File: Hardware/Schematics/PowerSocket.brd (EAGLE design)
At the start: 100 x 50 mm, 74 parts, among them IC1 ACS712-LC, IC2 ACS712-LC, IC3 ACS712-LC, T1 BT138-V, T2 BT138-V, T3 BT138-V, T4 BT138-V, T5 BT138-V, T6 BT138-V

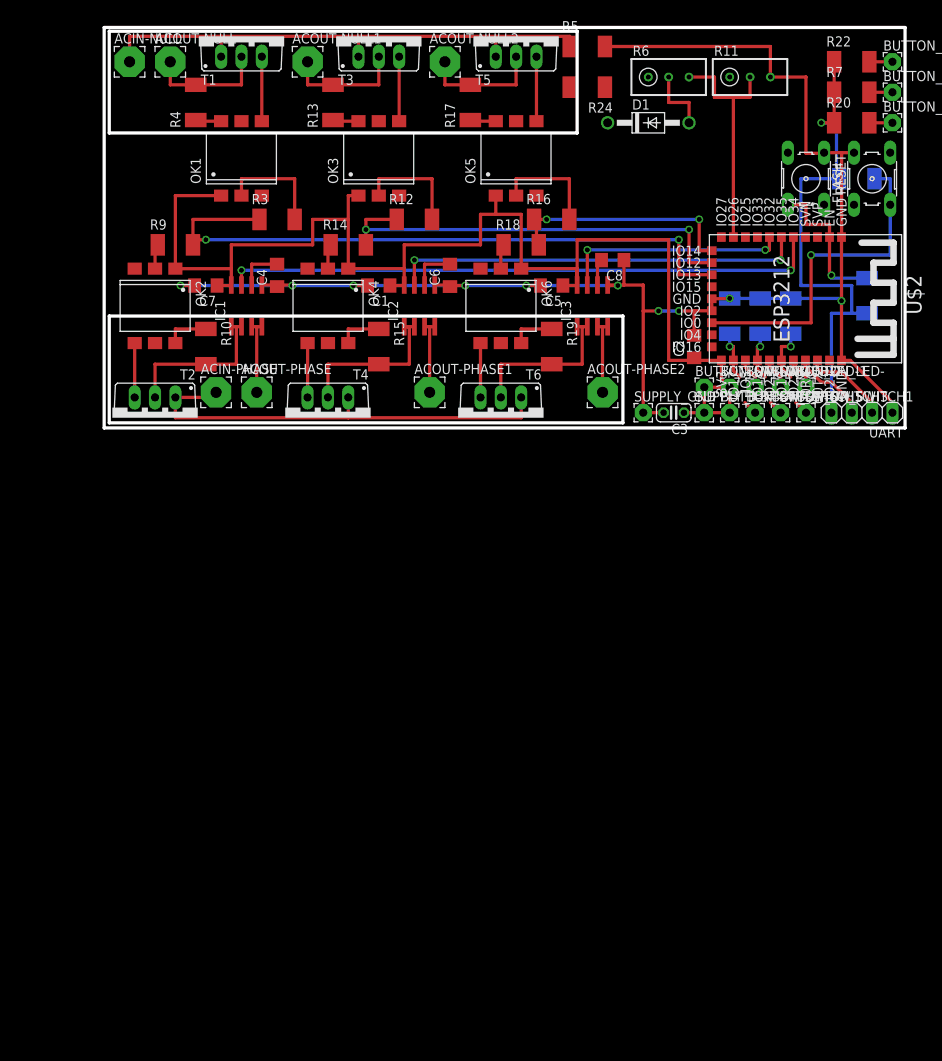
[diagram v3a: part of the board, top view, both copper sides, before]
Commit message: Schematic changes: Added JTAG pins. Changed some resistors to 0805 type. Only use 3 holes for the buttons. Changed current sensor to 3.3V tolerant ACS710. Some rewiring needed on board.
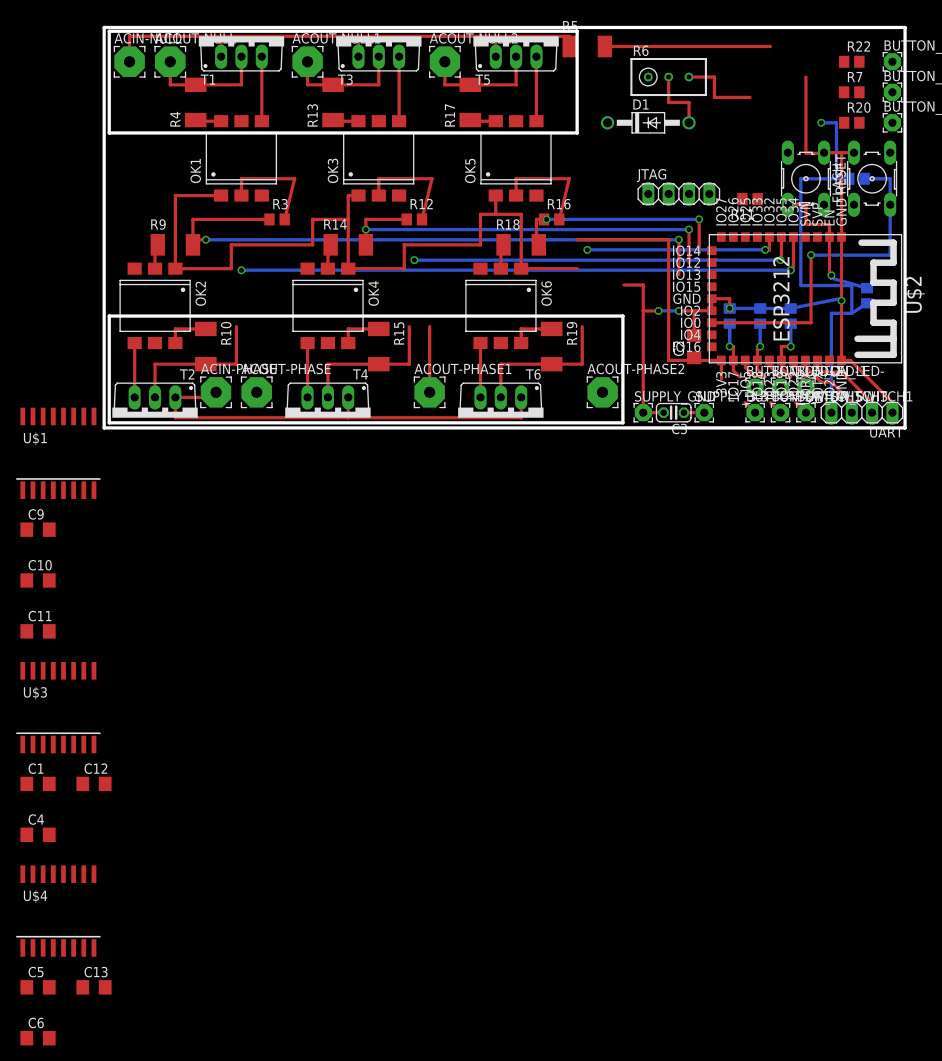
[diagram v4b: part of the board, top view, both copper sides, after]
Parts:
- removed BUTTON_SWITCH2, BUTTON_SWITCH4, BUTTON_SWITCH6: -, wirepad:2,15/1,0
- removed C7: 100nF, rcl:C1206
- removed C8: 470nF, rcl:C1206
- removed IC1, IC2, IC3: ACS712-LC, allegro-2:SOIC8
- removed R24: 0, eagle-ltspice:R2010
- added C10: 1nF, rcl:C1206
- added C11, C12, C13: 100nF, rcl:C1206
- added C9: 470nF, rcl:C1206
- added JTAG: -, pinhead:1X04
- added U$1, U$3, U$4: ACS710, PowerSocket:SO-16DW
- BUTTON_LED+: value - -> BUTTON_VCC
- C1, C5: value 100nF -> 470nF
- C4, C6: value 470nF -> 1nF
- R1, R12, R16, R2, R20, R21, R22, R23, R3, R7, R8: device eagle-ltspice:R2010 -> rcl:R0805
- R11: device rcl:RTRIM3296W -> rcl:R0805
- moved C5 108.6 mm to (-8.26, -69.8), turned to 0 degrees
- moved C6 108.3 mm to (-8.26, -76.2), turned to 0 degrees
- moved C4 76.0 mm to (-8.26, -50.8), turned to 0 degrees
- moved C1 75.4 mm to (-8.26, -44.5), turned to 0 degrees
- moved R11 15.2 mm to (80.6, 28.6), turned to 180 degrees
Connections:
- removed net N$27: IC2.7, U$2.IO35
- removed net N$37: BUTTON_LED+2.1, R22.2
- removed net N$40: C8.2, IC3.6
- removed net N$50: ACOUT-PHASE2.1, IC3.3, IC3.4
- new net N$55: C9.2, U$1.11
- new net N$56: JTAG.4, U$2.IO14
- new net N$57: JTAG.3, U$2.IO12
- new net N$58: JTAG.2, U$2.IO13
- new net N$59: JTAG.1, U$2.IO15
- new net N$60: C10.2, U$1.10
- new net N$61: U$3.5, U$3.6, U$3.7, U$3.8
- new net N$62: C1.2, U$3.11
- new net N$63: C4.2, U$3.10
- new net N$64: C5.2, U$4.11
- new net N$65: C6.2, U$4.10
- new net NFAULT: U$1.13, U$3.13, U$4.13
- net GND: now also C1.1, C10.1, C11.1, C12.1, C13.1, C5.1, C9.1, R11.2, U$1.16, U$1.9, U$3.16, U$3.9, U$4.16, U$4.9; no longer C1.2, C5.2, C7.2, C8.1, IC1.5, IC2.5, IC3.5, R11.3
- net N$11: now also U$2.IO35, U$3.12; no longer C4.2, IC1.6
- net N$12: now also U$1.12; no longer IC1.7
- net N$13: now also U$1.5, U$1.6, U$1.7, U$1.8; no longer IC1.3, IC1.4
- net N$15: now also BUTTON_LED-.1, R7.1; no longer BUTTON_LED+.1, R7.2
- net N$16: now also BUTTON_LED-1.1, R20.1; no longer BUTTON_LED+1.1, R20.2
- net N$23: now also U$1.1, U$1.2, U$1.3, U$1.4; no longer IC1.1, IC1.2
- net N$25: now also U$2.IO26; no longer U$2.IO12
- net N$26: now also BUTTON_LED-2.1, R22.1; no longer C6.2, IC2.6
- net N$3: now also R11.1, U$2.IO33; no longer R11.2, U$2.IO26
- net N$31: now also R20.2; no longer BUTTON_LED-1.1
- net N$35: now also U$4.5, U$4.6, U$4.7, U$4.8; no longer IC2.1, IC2.2, R15.2, T4.T2
- net N$36: no longer IC2.3, IC2.4
- net N$41: now also U$4.12; no longer IC3.7
- net N$49: now also U$4.1, U$4.2, U$4.3, U$4.4; no longer IC3.1, IC3.2
- net N$51: now also D1.C; no longer R24.2
- net N$52: now also R22.2; no longer BUTTON_LED-2.1
- net N$53: now also R15.2, T4.T2, U$3.1, U$3.2, U$3.3, U$3.4; no longer D1.C, R24.1
- net N$54: now also U$2.IO27; no longer U$2.IO14
- net N$8: now also U$2.IO25; no longer U$2.IO13
- net N$9: now also R7.2; no longer BUTTON_LED-.1
- net VCC: now also BUTTON_LED+.1, BUTTON_LED+1.1, BUTTON_LED+2.1, C11.2, C12.2, C13.2, U$1.14, U$1.15, U$3.14, U$3.15, U$4.14, U$4.15; no longer BUTTON_SWITCH2.1, BUTTON_SWITCH4.1, BUTTON_SWITCH6.1, C1.1, C5.1, C7.1, IC1.8, IC2.8, IC3.8, R20.1, R22.1, R7.1
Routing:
- net GND: track 205.4 -> 123.8 mm, vias 10 -> 4
- net N$27: track 51.8 -> 0.00 mm, vias 2 -> 0
- net N$11: track 5.79 -> 48.7 mm, vias 0 -> 2
- net VCC: track 231.4 -> 193.2 mm
- net N$35: track 20.9 -> 0.00 mm
- net N$3: track 30.1 -> 10.2 mm
- net N$53: track 0.00 -> 19.0 mm
- net N$50: track 9.47 -> 0.00 mm
- net N$13: track 9.46 -> 0.00 mm
- net N$26: track 5.78 -> 0.00 mm
- net N$41: track 28.7 -> 24.3 mm
- net N$40: track 3.62 -> 0.00 mm
- net N$37: track 2.88 -> 0.00 mm
- net N$16: track 2.88 -> 0.00 mm
- net N$15: track 2.88 -> 0.00 mm
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
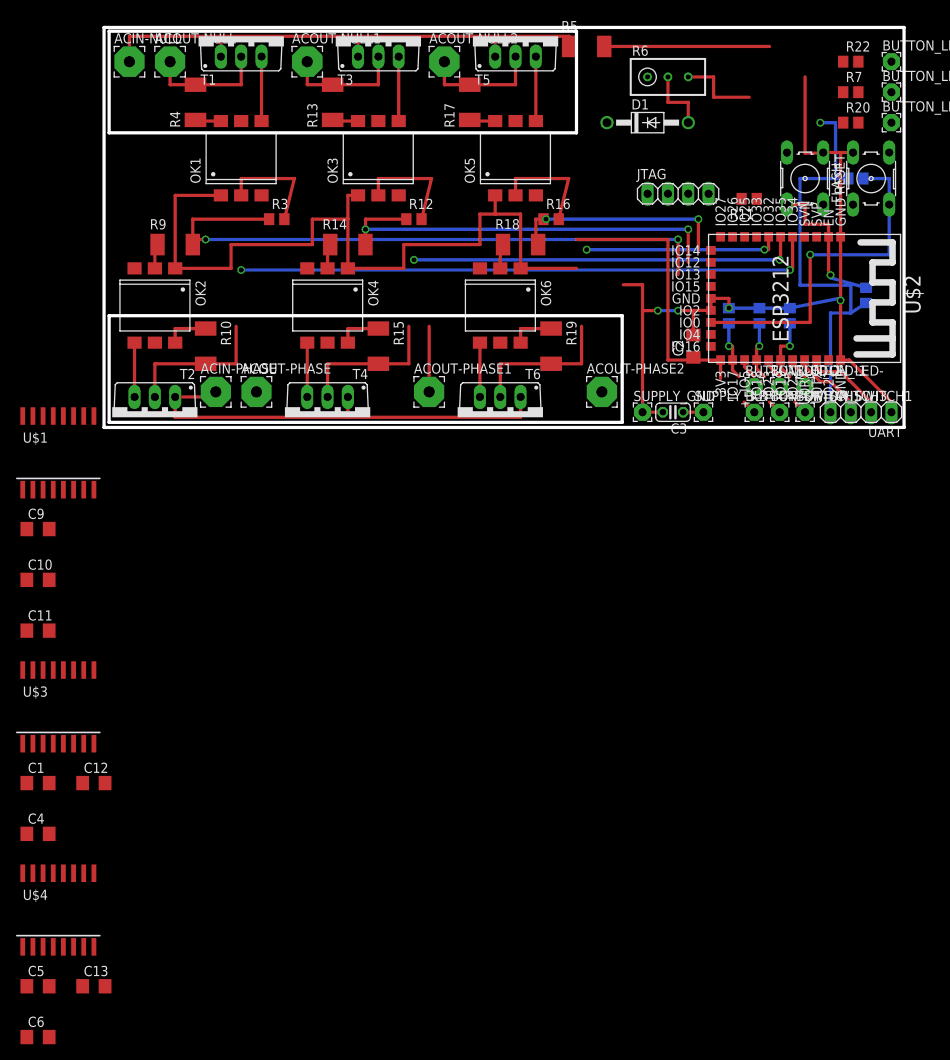
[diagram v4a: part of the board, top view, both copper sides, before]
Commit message: Did some routing of the board.
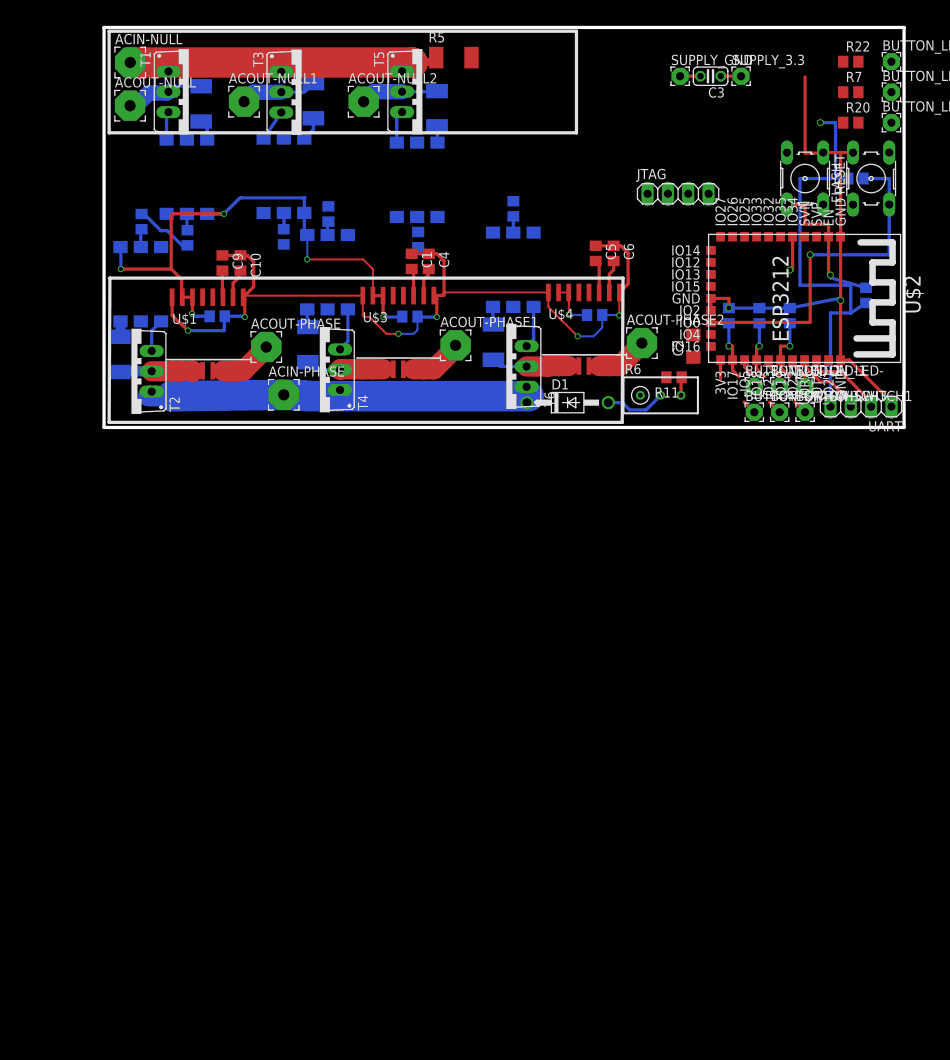
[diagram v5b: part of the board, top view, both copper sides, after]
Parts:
- C1, C10, C11, C12, C13, C4, C5, C6, C9: device rcl:C1206 -> rcl:C0805
- R14, R18: device eagle-ltspice:R2010 -> rcl:C0805
- R9: device eagle-ltspice:R2010 -> rcl:R0805
- moved C6 121.5 mm to (63.7, 21.8), turned to 270 degrees
- moved C5 115.1 mm to (61.5, 21.8), turned to 270 degrees
- moved C13 104.7 mm to (61.3, 14.1), flipped to the bottom
- moved U$4 97.9 mm to (60.0, 12.3)
- moved C4 86.6 mm to (40.6, 20.8), turned to 270 degrees
- moved C1 80.2 mm to (38.5, 20.8), turned to 270 degrees
- moved C12 70.4 mm to (38.2, 13.8), flipped to the bottom
- moved U$3 63.2 mm to (36.8, 11.9)
- moved C10 47.0 mm to (17.1, 20.6), turned to 270 degrees
- moved C11 45.2 mm to (14.1, 13.9), flipped to the bottom
- moved C3 42.3 mm to (75.8, 43.9)
- moved SUPPLY_3.3 42.3 mm to (79.6, 43.9)
- moved SUPPLY_GND 42.3 mm to (72.0, 43.9)
- moved C9 40.5 mm to (14.8, 20.6), turned to 270 degrees
- moved R6 39.8 mm to (69.6, 4.01)
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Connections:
- removed net N$61: U$3.5, U$3.6, U$3.7, U$3.8
- removed net NFAULT: U$1.13, U$3.13, U$4.13
- new net N$27: U$1.13
- new net N$40: U$3.13
- new net N$50: U$4.13
- net N$35: now also ACOUT-PHASE2.1
- net N$36: now also U$3.5, U$3.6, U$3.7, U$3.8
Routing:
- net N$8: track 77.8 -> 7.15 mm, vias 2 -> 0
- net N$12: track 73.1 -> 4.49 mm, vias 2 -> 1
- net GND: track 123.8 -> 180.6 mm, vias 4 -> 8
- net N$25: track 52.8 -> 0.00 mm, vias 2 -> 0
- net VCC: track 193.2 -> 140.7 mm, vias 1 -> 7
- net N$11: track 48.7 -> 0.00 mm, vias 2 -> 0
- net N$54: track 27.7 -> 0.00 mm, vias 2 -> 0
- net N$41: track 24.3 -> 0.00 mm, vias 2 -> 0
- net N$42: track 14.0 -> 0.00 mm
- net N$28: track 14.0 -> 2.03 mm
- net N$6: track 14.0 -> 2.06 mm
- net N$23: track 19.0 -> 10.6 mm
- net N$13: track 0.00 -> 7.98 mm
- net N$49: track 19.0 -> 11.0 mm
- net N$53: track 19.0 -> 11.1 mm
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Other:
- outline, holes or cut-outs redrawn

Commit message: Routed board.
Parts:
- moved BUTTON_LED+2 42.8 mm to (91.8, 3.42)
- moved BUTTON_LED+ 38.5 mm to (95.1, 3.51)
- moved R22 36.3 mm to (78.6, 12.5), turned to 90 degrees
- moved BUTTON_LED+1 34.6 mm to (98.2, 3.50)
- moved R7 29.3 mm to (88.0, 13.1), turned to 135 degrees
- moved R1 28.0 mm to (84.5, 42.4), turned to 0 degrees
- moved R20 26.5 mm to (82.9, 13.7), turned to 90 degrees
- moved R2 12.1 mm to (97.1, 42.8)
- moved RESET 11.8 mm to (88.3, 42.9)
- moved FLASH 11.8 mm to (95.9, 42.9)
- moved C2 11.6 mm to (69.4, 21.0)
- moved C3 10.9 mm to (65.1, 46.2)
- moved SUPPLY_3.3 10.9 mm to (68.9, 46.2)
- moved BUTTON_SWITCH5 10.8 mm to (73.4, 9.21)
- moved SUPPLY_GND 10.7 mm to (61.5, 46.2)
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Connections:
- net N$3: now also U$2.IO4; no longer U$2.IO33
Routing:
- net VCC: track 140.7 -> 259.1 mm, vias 7 -> 10
- net N$12: track 4.49 -> 95.3 mm, vias 1 -> 0
- net N$8: track 7.15 -> 88.5 mm, vias 0 -> 3
- net N$11: track 0.00 -> 76.8 mm
- net N$25: track 0.00 -> 71.1 mm, vias 0 -> 3
- net GND: track 180.6 -> 232.6 mm, vias 8 -> 10
- net N$54: track 0.00 -> 47.7 mm, vias 0 -> 1
- net N$41: track 0.00 -> 44.1 mm, vias 0 -> 2
- net N$3: track 2.27 -> 20.4 mm, vias 0 -> 1
- net N$2: track 19.2 -> 11.6 mm, vias 1 -> 0
- net N$59: track 0.00 -> 5.82 mm
- net N$56: track 0.00 -> 5.35 mm
- net N$58: track 0.00 -> 5.34 mm
- net N$7: track 43.5 -> 38.3 mm, vias 1 -> 2
- net N$39: track 9.26 -> 14.4 mm
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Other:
- board size 100 x 50 mm -> 100 x 47.6 mm

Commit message: Some Routing improvements.
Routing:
- net N$8: track 88.5 -> 101.6 mm, vias 3 -> 1
- net N$41: track 44.1 -> 41.9 mm
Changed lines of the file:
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@@
 <wire x1="10.1" y1="22.4" x2="10.435" y2="22.4" width="0.4064" layer="16"/>
 <wire x1="10.435" y1="22.4" x2="10.435" y2="22.76" width="0.4064" layer="16"/>
-<wire x1="79.765" y1="32.83" x2="79.765" y2="35.035" width="0.4064" layer="1"/>
-<wire x1="79.765" y1="35.035" x2="77.7" y2="37.1" width="0.4064" layer="1"/>
-<wire x1="77.7" y1="37.1" x2="77.5" y2="37.3" width="0.4064" layer="1"/>
-<wire x1="10.435" y1="22.76" x2="10.595" y2="22.6" width="0.4064" layer="16"/>
-<wire x1="10.595" y1="22.6" x2="17.6" y2="22.6" width="0.4064" layer="16"/>
-<wire x1="17.6" y1="22.6" x2="18" y2="23" width="0.4064" layer="16"/>
-<wire x1="18" y1="23" x2="18" y2="24.8" width="0.4064" layer="16"/>
-<via x="18" y="24.8" extent="1-16" drill="0.6" shape="square"/>
-<wire x1="18" y1="24.8" x2="24.8" y2="31.6" width="0.4064" layer="1"/>
-<wire x1="24.8" y1="31.6" x2="28.8" y2="31.6" width="0.4064" layer="1"/>
-<via x="28.8" y="31.6" extent="1-16" drill="0.6" shape="square"/>
-<wire x1="28.8" y1="31.6" x2="29.8" y2="30.6" width="0.4064" layer="16"/>
-<wire x1="29.8" y1="30.6" x2="46.3" y2="30.6" width="0.4064" layer="16"/>
-<wire x1="46.3" y1="30.6" x2="52.6" y2="36.9" width="0.4064" layer="16"/>
-<wire x1="52.6" y1="36.9" x2="59.1" y2="36.9" width="0.4064" layer="16"/>
-<via x="59.1" y="36.9" extent="1-16" drill="0.6" shape="square"/>
-<wire x1="59.1" y1="36.9" x2="59.3" y2="37.1" width="0.4064" layer="1"/>
-<wire x1="59.3" y1="37.1" x2="77.7" y2="37.1" width="0.4064" layer="1"/>
+<wire x1="10.435" y1="22.76" x2="20.3" y2="22.76" width="0.4064" layer="16"/>
+<wire x1="20.3" y1="22.76" x2="20.3" y2="19.7" width="0.4064" layer="16"/>
+<wire x1="20.3" y1="19.7" x2="62.6" y2="19.7" width="0.4064" layer="16"/>
+<wire x1="62.6" y1="19.7" x2="62.6" y2="36.9" width="0.4064" layer="16"/>
+<wire x1="62.6" y1="36.9" x2="79.8" y2="36.9" width="0.4064" layer="16"/>
+<wire x1="79.8" y1="36.9" x2="79.8" y2="34.8" width="0.4064" layer="16"/>
+<via x="79.8" y="34.8" extent="1-16" drill="0.6" shape="square"/>
+<wire x1="79.8" y1="34.8" x2="79.765" y2="34.8" width="0.4064" layer="1"/>
+<wire x1="79.765" y1="34.8" x2="79.765" y2="32.83" width="0.4064" layer="1"/>
 </signal>
 <signal name="N$12">
@@
 <wire x1="60.9" y1="28.2" x2="63.7" y2="28.2" width="0.4064" layer="1"/>
 <via x="63.7" y="28.2" extent="1-16" drill="0.6" shape="square"/>
-<wire x1="63.7" y1="28.2" x2="63.7" y2="27.5" width="0.4064" layer="16"/>
-<wire x1="63.7" y1="27.5" x2="70.3" y2="20.9" width="0.4064" layer="16"/>
-<wire x1="70.3" y1="20.9" x2="70.5" y2="20.9" width="0.4064" layer="16"/>
-<wire x1="70.5" y1="20.9" x2="80.6" y2="31" width="0.4064" layer="16"/>
-<wire x1="80.6" y1="31" x2="82.8" y2="31" width="0.4064" layer="16"/>
+<wire x1="63.7" y1="28.2" x2="63.9" y2="28.5" width="0.4064" layer="16"/>
+<wire x1="63.9" y1="28.5" x2="69" y2="35.1" width="0.4064" layer="16"/>
+<wire x1="69" y1="35.1" x2="71.7" y2="35.1" width="0.4064" layer="16"/>
+<wire x1="71.7" y1="35.1" x2="74.7" y2="31" width="0.4064" layer="16"/>
+<wire x1="74.7" y1="31" x2="82.8" y2="31" width="0.4064" layer="16"/>
 <via x="82.8" y="31" extent="1-16" drill="0.6" shape="square"/>
 <wire x1="82.8" y1="31" x2="82.765" y2="31" width="0.4064" layer="1"/>
